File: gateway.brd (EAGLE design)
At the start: 100 x 146 mm, 68 parts, among them J1 RASPBERRYPI-40-PIN-GPIO_PTH_N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, Q1 BSS123

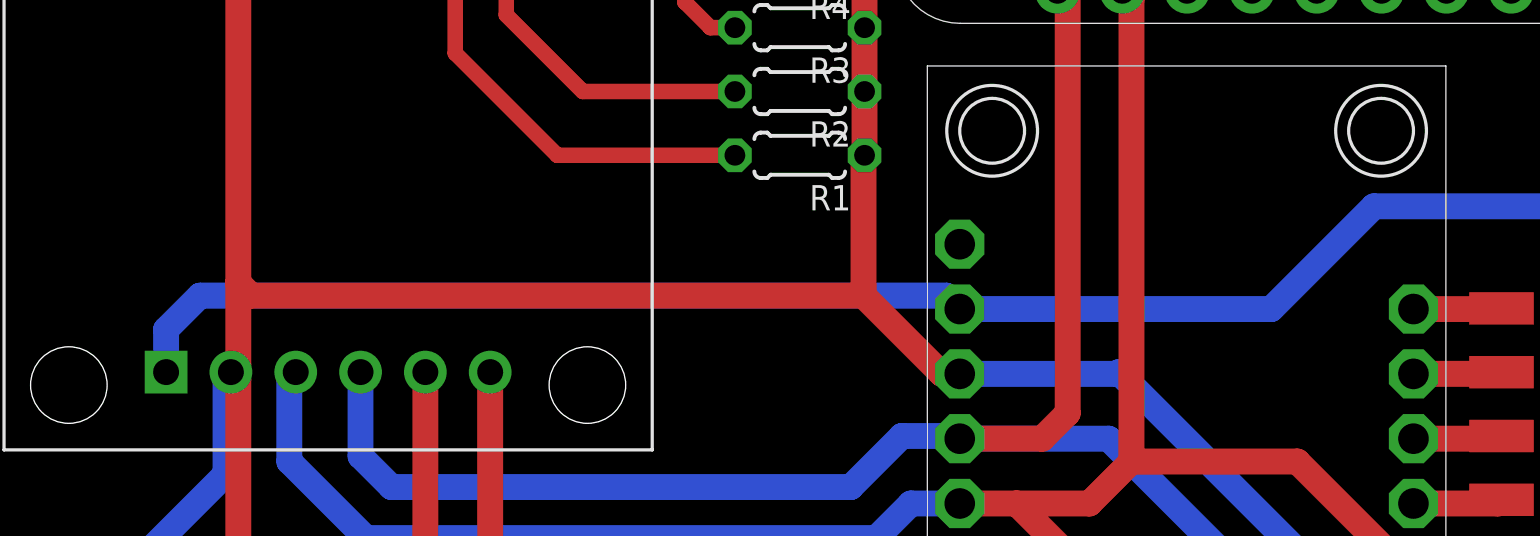
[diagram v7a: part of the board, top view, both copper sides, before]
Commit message: changed bno05 vin / 3.3V connection
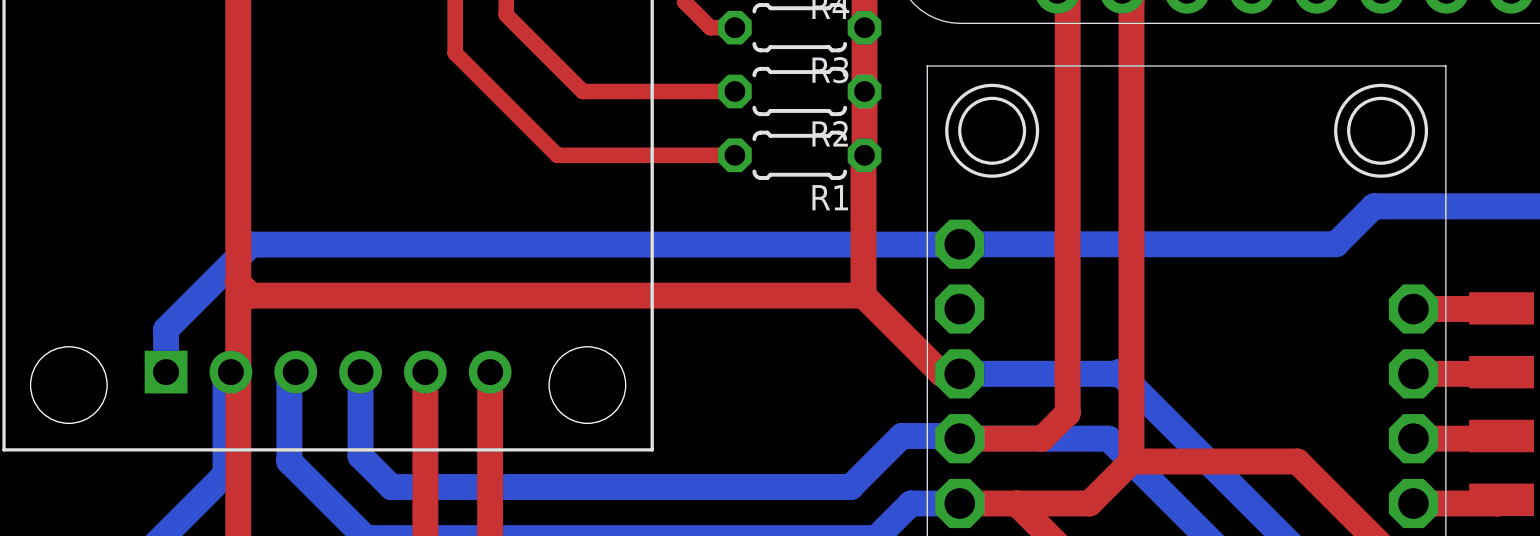
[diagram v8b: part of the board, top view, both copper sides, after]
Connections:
- removed net VIN: U$4.VIN
- net FEATHER_3.3V: now also U$4.VIN; no longer U$4.3V3
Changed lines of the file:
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@@
 <signal name="FEATHER_3.3V">
 <contactref element="MS1" pad="2"/>
-<contactref element="U$4" pad="3V3"/>
 <contactref element="INA219" pad="P$1"/>
-<wire x1="46.27" y1="105.475" x2="58.475" y2="105.475" width="1.016" layer="16"/>
-<wire x1="58.475" y1="105.475" x2="62.5" y2="109.5" width="1.016" layer="16"/>
 <wire x1="33.5" y1="14.5" x2="84.5" y2="14.5" width="1.016" layer="16"/>
 <wire x1="84.5" y1="14.5" x2="88" y2="18" width="1.016" layer="16"/>
@@
 <wire x1="32.5" y1="15.5" x2="33.5" y2="14.5" width="1.016" layer="16"/>
 <wire x1="15.17" y1="103.004" x2="15.17" y2="104.67" width="1.016" layer="16"/>
-<wire x1="15.17" y1="104.67" x2="16.5" y2="106" width="1.016" layer="16"/>
-<wire x1="46.245" y1="105.5" x2="46.27" y2="105.475" width="1.016" layer="16"/>
 <wire x1="62.5" y1="109.5" x2="85.5" y2="109.5" width="1.016" layer="16"/>
 <wire x1="85.5" y1="109.5" x2="88" y2="112" width="1.016" layer="16"/>
@@
 <wire x1="85.5" y1="135.5" x2="85.5" y2="138.1" width="1.016" layer="16"/>
 <wire x1="85.5" y1="138.1" x2="85.66" y2="138.26" width="1.016" layer="16"/>
-<wire x1="16.5" y1="106" x2="45.745" y2="106" width="1.016" layer="16"/>
-<wire x1="45.745" y1="106" x2="46.27" y2="105.475" width="1.016" layer="16"/>
 <contactref element="RTC" pad="5"/>
 <wire x1="83" y1="89.92" x2="87.08" y2="89.92" width="1.016" layer="16"/>
 <wire x1="87.08" y1="89.92" x2="88" y2="89" width="1.016" layer="16"/>
-</signal>
-<signal name="VIN">
 <contactref element="U$4" pad="VIN"/>
+<wire x1="15.17" y1="104.67" x2="18.5" y2="108" width="1.016" layer="16"/>
+<wire x1="18.5" y1="108" x2="46.255" y2="108" width="1.016" layer="16"/>
+<wire x1="46.255" y1="108" x2="46.27" y2="108.015" width="1.016" layer="16"/>
+<wire x1="46.27" y1="108.015" x2="61.015" y2="108.015" width="1.016" layer="16"/>
+<wire x1="61.015" y1="108.015" x2="62.5" y2="109.5" width="1.016" layer="16"/>
 </signal>
 <signal name="EN">
